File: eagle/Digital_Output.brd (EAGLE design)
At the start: 42.9 x 33 mm, 19 parts, among them IC2 NJU7032, T1 2SK4017, T2 2SK4017

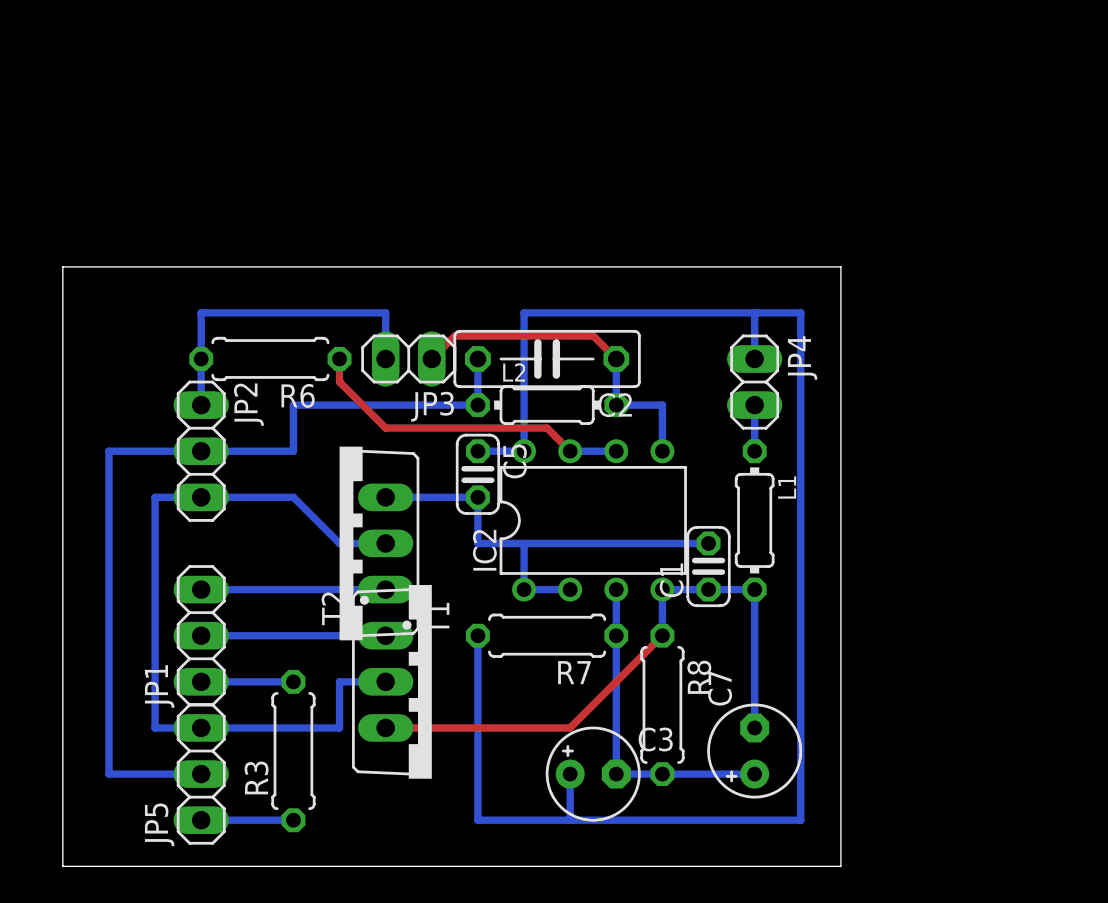
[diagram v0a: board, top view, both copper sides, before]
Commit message: 出力部のEagleファイルを変更
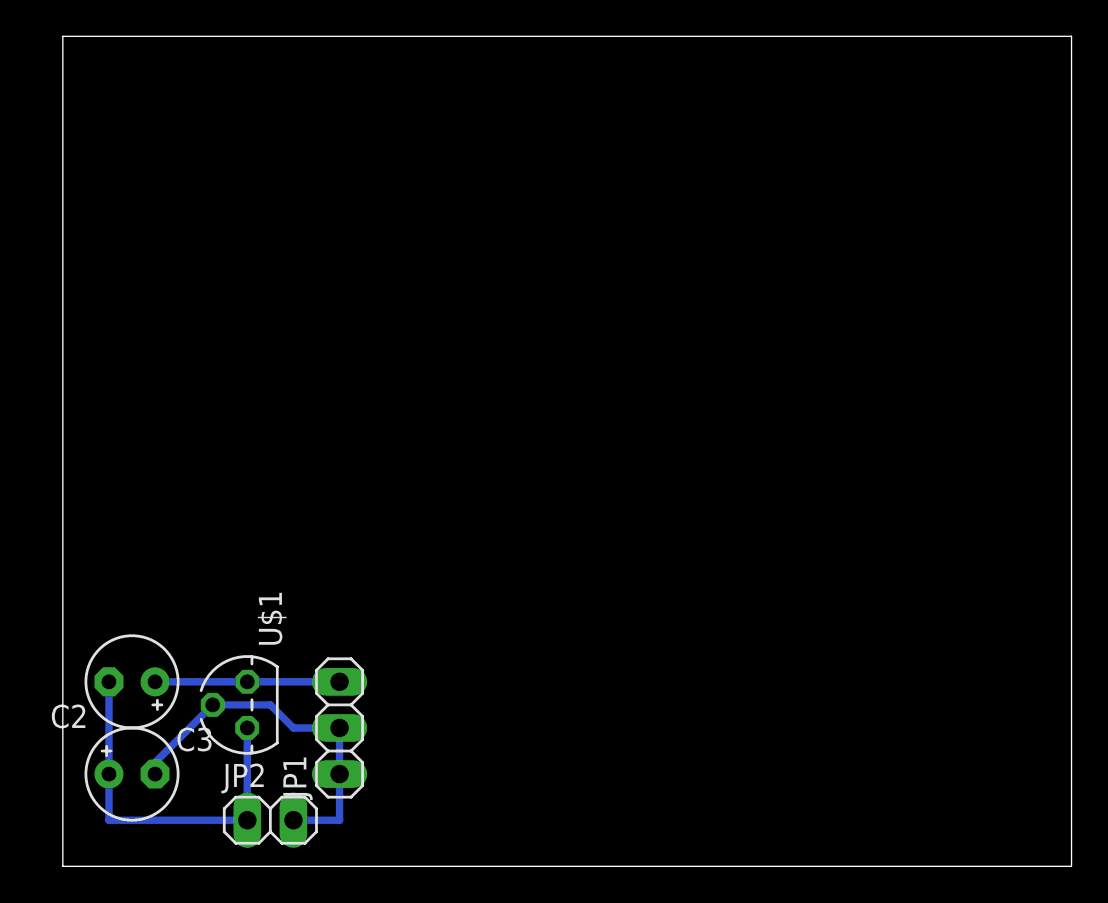
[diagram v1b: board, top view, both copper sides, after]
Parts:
- removed C1, C5: 0.1uF, rcl:C025-024X044
- removed C7: 100uF, rcl:E2,5-5
- removed IC2: NJU7032, linear:DIL08
- removed JP3: BYPASS_BUFFER, pinhead:1X02
- removed JP4: 5VIN, pinhead:1X02
- removed JP5: Level, pinhead:1X03
- removed L1, L2: 1uH, rcl:0204/7
- removed R3: 1k, rcl:0207/7
- removed R6: 47, rcl:0207/7
- removed R7, R8: 10k, rcl:0207/7
- removed T1, T2: 2SK4017, transistor-power:TO220BV
- added U$1: TLE2426CLP, tle2426:TO226AA
- C2: value 100p -> 10uF; device rcl:C075-032X103 -> rcl:E2,5-5
- C3: value 100uF -> 10uF
- JP1: value DIGITAL_IN -> PWRIN
- JP2: value OUT -> PWROUT; device pinhead:1X03 -> pinhead:1X02
- moved C2 29.0 mm to (3.81, 10.2)
- moved C3 25.4 mm to (3.81, 5.08)
- moved JP2 20.7 mm to (11.4, 2.54), turned to 0 degrees
- moved JP1 9.16 mm to (15.2, 7.62)
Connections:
- removed net +5V: C3.+, C5.1, IC2.8, JP4.1, R7.2
- removed net AGND: C1.1, C7.-, IC2.4, L1.2, R8.1, T2.S
- removed net BUFFERD: JP2.1, JP3.2, R6.2
- removed net BYPASS: C2.2, JP2.2, JP5.2, L2.1
- removed net GND_OUT: JP2.3, JP5.3, T1.D, T2.D
- removed net N$1: C2.1, IC2.5, JP3.1, L2.2
- removed net N$16: IC2.6, IC2.7, R6.1
- removed net N$17: C3.-, C7.+, IC2.3, R7.1, R8.2
- removed net N$8: JP5.1, R3.1
- removed net SW_GND: JP1.2, T2.G
- removed net SW_VGND: JP1.3, T1.G
- removed net VGND: C1.2, C5.2, IC2.1, IC2.2, T1.S
- removed net WAVE_OUT: JP1.1, R3.2
- new net VCC: C2.+, JP1.3, U$1.3
- new net VCC/2: C2.-, C3.+, JP2.1, U$1.1
- net GND: now also C3.-, JP1.1, JP1.2, JP2.2, U$1.2; no longer JP4.2, L1.1
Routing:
- net +5V: track 86.4 -> 0.00 mm
- net BYPASS: track 48.3 -> 0.00 mm
- net GND_OUT: track 41.7 -> 0.00 mm
- net AGND: track 32.6 -> 0.00 mm
- net VGND: track 25.4 -> 0.00 mm
- net VCC/2: track 0.00 -> 20.3 mm
- net N$1: track 18.8 -> 0.00 mm
- net N$16: track 18.1 -> 0.00 mm
- net N$17: track 17.8 -> 0.00 mm
- net BUFFERD: track 17.8 -> 0.00 mm
- net GND: track 2.54 -> 20.3 mm
- net VCC: track 0.00 -> 10.2 mm
- net SW_VGND: track 10.2 -> 0.00 mm
- net SW_GND: track 10.2 -> 0.00 mm
- net WAVE_OUT: track 5.08 -> 0.00 mm
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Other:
- board size 42.9 x 33 mm -> 55.5 x 45.7 mm
